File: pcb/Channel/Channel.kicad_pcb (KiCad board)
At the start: 2 copper layers, 32 x 43.5 mm, 11 parts, among them J1 Mainboard, J2 SPI_CHAIN_IN, J3 SPI_CHAIN_OUT, J4 Motor_Out, J6 Motor_In, SW1 RotaryEncoder_Switch

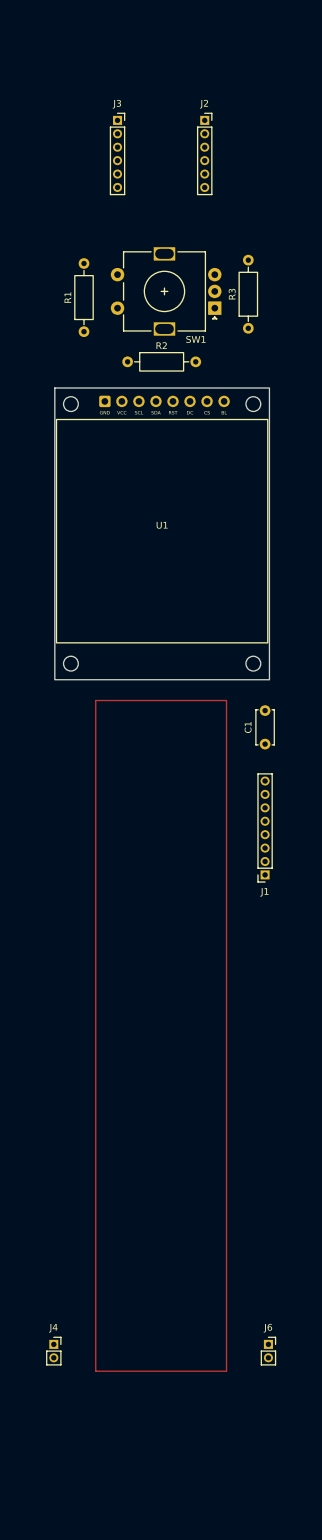
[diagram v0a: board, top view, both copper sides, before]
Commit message: Update main pcb silkscreen.
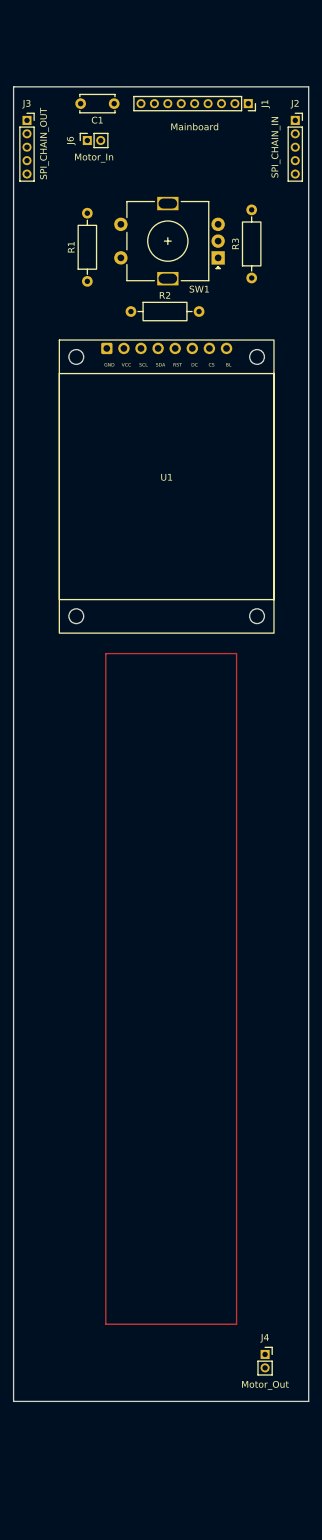
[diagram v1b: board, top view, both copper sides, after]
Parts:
- J1: footprint Connector_PinSocket_2.00mm:PinSocket_1x08_P2.00mm_Vertical -> Connector_PinSocket_2.00mm:PinSocket_1x09_P2.00mm_Vertical
- J2, J3: footprint Connector_PinSocket_2.00mm:PinSocket_1x06_P2.00mm_Vertical -> Connector_PinSocket_2.00mm:PinSocket_1x05_P2.00mm_Vertical
- moved J6 181.5 mm to (56.0, 52.0), turned to 90 degrees
- moved J1 115.0 mm to (80.0, 46.5), turned to -90 degrees
- moved C1 98.1 mm to (60.0, 46.5), turned to 180 degrees
- moved J4 31.5 mm to (82.5, 233.0)
- moved J2 13.5 mm to (87.0, 49.0)
- moved J3 13.5 mm to (47.0, 49.0)
- moved R1 7.52 mm to (56.0, 73.0)
- moved R2 7.52 mm to (62.5, 77.5)
- moved R3 7.52 mm to (80.5, 72.5)
- moved SW1 7.52 mm to (75.5, 69.5)
- moved U1 7.18 mm to (51.8, 81.8)
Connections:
- J2 pad 5: SHARED_RST -> SCR_BL_PWM
- J3 pad 5: SHARED_RST -> SCR_BL_PWM
- U1 pad 5: SHARED_RST -> SCREEN_RST
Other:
- board size 32 x 43.5 mm -> 44 x 196 mm

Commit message: Silkscreen updates.
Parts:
- added G***: LOGO, LOGO, F.Cu at (53.5, 233.0)

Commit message: Fix up channel pcb
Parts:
- added F1: ~, Behringer X32 Fader:Behringer X32 Fader, F.Cu at (59.0, 98.6)
- added Mount_1: MountingHole_3.2mm_M3, MountingHole:MountingHole_3.2mm_M3, F.Cu at (53.0, 36.8)
- added Mount_2: MountingHole_3.2mm_M3, MountingHole:MountingHole_3.2mm_M3, F.Cu at (81.5, 36.8)
- added Mount_3: MountingHole_3.2mm_M3, MountingHole:MountingHole_3.2mm_M3, F.Cu at (53.0, 170.0)
- added Mount_4: MountingHole_3.2mm_M3, MountingHole:MountingHole_3.2mm_M3, F.Cu at (81.5, 170.0)
- added Mount_6: MountingHole_3.2mm_M3, MountingHole:MountingHole_3.2mm_M3, F.Cu at (53.0, 229.2)
- added Mount_7: MountingHole_3.2mm_M3, MountingHole:MountingHole_3.2mm_M3, F.Cu at (81.5, 229.0)
- C1, J1, J2, J3: moved to B.Cu
- moved J6 157.5 mm to (81.0, 207.5), turned to 180 degrees
- moved U1 28.5 mm to (51.1, 53.2)
- moved SW1 26.6 mm to (74.5, 42.9)
- moved R2 26.0 mm to (62.2, 51.5)
- moved J1 22.3 mm to (64.0, 62.0)
- moved R1 21.3 mm to (56.8, 51.8)
- moved G*** 20.9 mm to (67.5, 217.5)
- moved R3 20.5 mm to (78.2, 52.1)
- moved C1 16.1 mm to (55.8, 62.0), turned to 0 degrees
- moved J4 15.6 mm to (81.0, 217.5)
- moved J3 7.43 mm to (52.0, 43.5), turned to 180 degrees
- moved J2 7.11 mm to (82.5, 43.5), turned to 180 degrees
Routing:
- net E_VCC: track 0.00 -> 251.3 mm
- net GND: track 0.00 -> 109.2 mm
- net FADER_OUT: track 0.00 -> 69.9 mm, vias 0 -> 1
- net SCR_BL_PWM: track 0.00 -> 45.8 mm, vias 0 -> 1
- net ENC_SW: track 0.00 -> 43.3 mm
- net SPI_SCK: track 0.00 -> 42.8 mm, vias 0 -> 1
- net ENC_CLK: track 0.00 -> 38.4 mm
- net SPI_MOSI: track 0.00 -> 34.9 mm
- net ENC_DT: track 0.00 -> 31.9 mm, vias 0 -> 1
- net SCREEN_CS: track 0.00 -> 15.4 mm
- net MOTOR-: track 0.00 -> 14.8 mm
- net SCREEN_RST: track 0.00 -> 14.8 mm
- net MOTOR+: track 0.00 -> 10.0 mm
- net SCREEN_DC: track 0.00 -> 7.87 mm
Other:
- board size 44 x 196 mm -> 34.5 x 202 mm

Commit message: Update pcb gerbers,
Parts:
- G***: moved to B.Cu
- moved G*** 0.58 mm to (67.0, 217.8), turned to 180 degrees

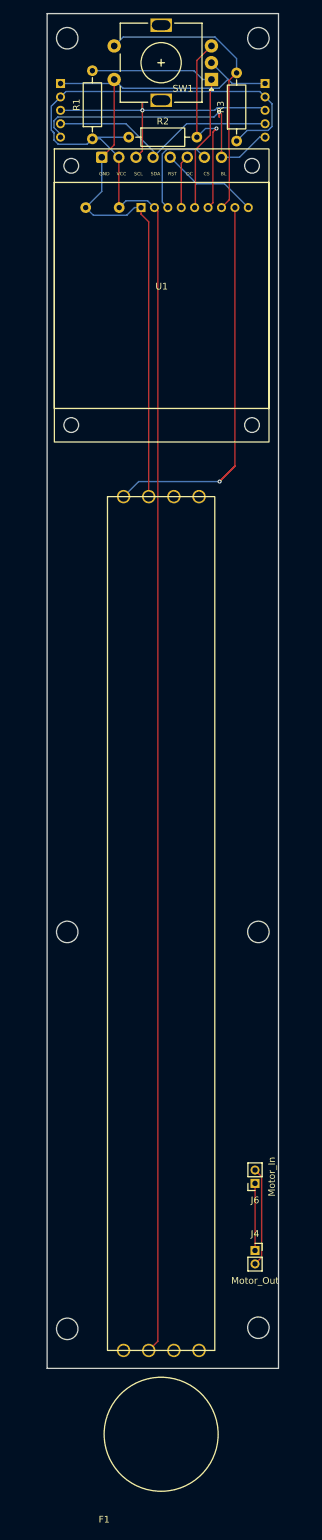
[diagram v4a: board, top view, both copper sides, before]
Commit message: Get firmware and sofware working better with hardware, in terms of all 5 channels and motorized faders.
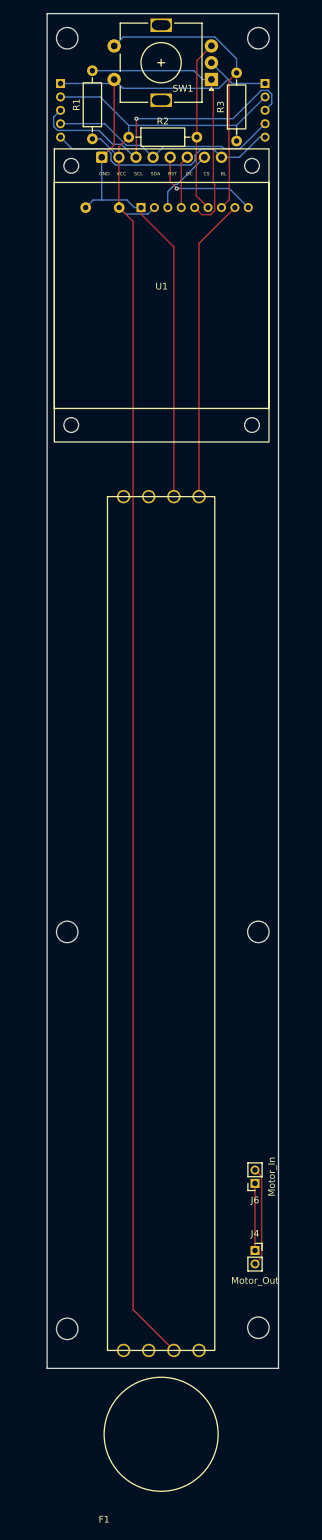
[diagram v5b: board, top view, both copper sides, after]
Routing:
- net FADER_OUT: track 69.9 -> 45.3 mm, vias 1 -> 0
- net E_VCC: track 251.3 -> 234.2 mm
- net SCR_BL_PWM: track 45.8 -> 36.1 mm, vias 1 -> 0
- net ENC_DT: track 31.9 -> 25.8 mm, vias 1 -> 0
- net SCREEN_CS: track 15.4 -> 9.95 mm
- net SPI_SCK: track 42.8 -> 47.8 mm
- net ENC_CLK: track 38.4 -> 41.7 mm
- net SCREEN_RST: track 14.8 -> 16.9 mm, vias 0 -> 1
- net GND: track 109.2 -> 108.6 mm
